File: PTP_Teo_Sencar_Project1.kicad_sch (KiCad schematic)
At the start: 0 parts

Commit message: Ispunjena sastavnica
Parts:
- added R1, R2: R_Small, symbol Device:R_Small
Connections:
- new net +3.3V: R2.1
- new net GND: R1.2
- new net U_izl: R1.1, R2.2
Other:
- company: (none) -> TVZ
- title: (none) -> BCD brojač

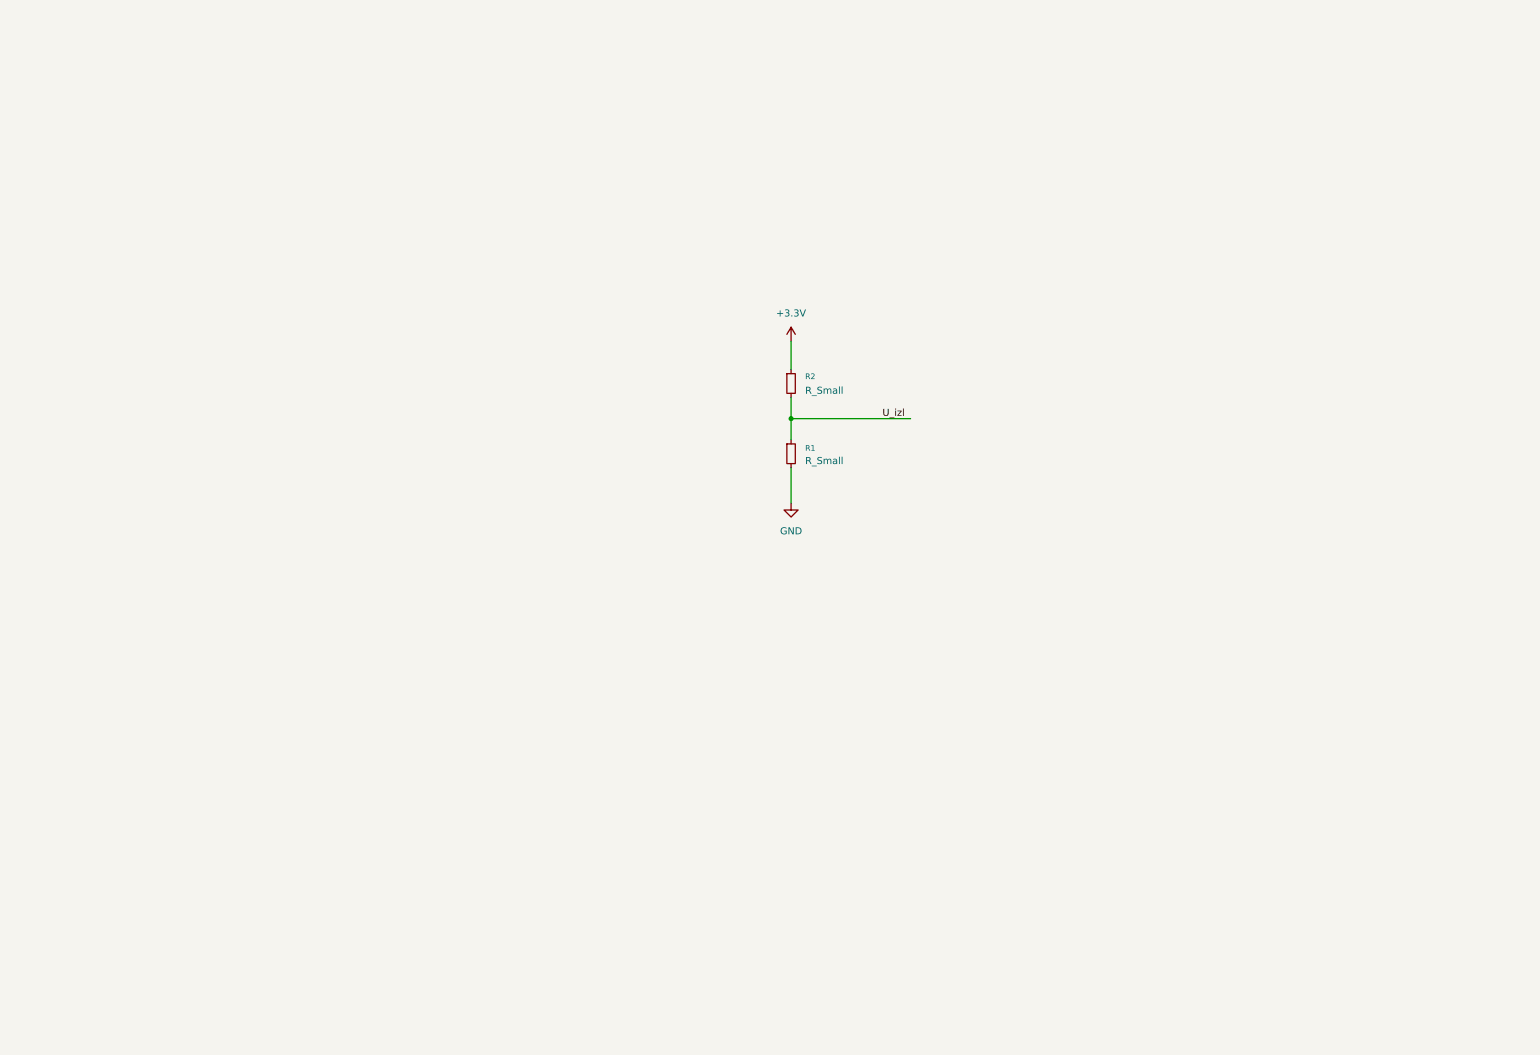
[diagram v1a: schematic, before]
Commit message: Dodan NE555
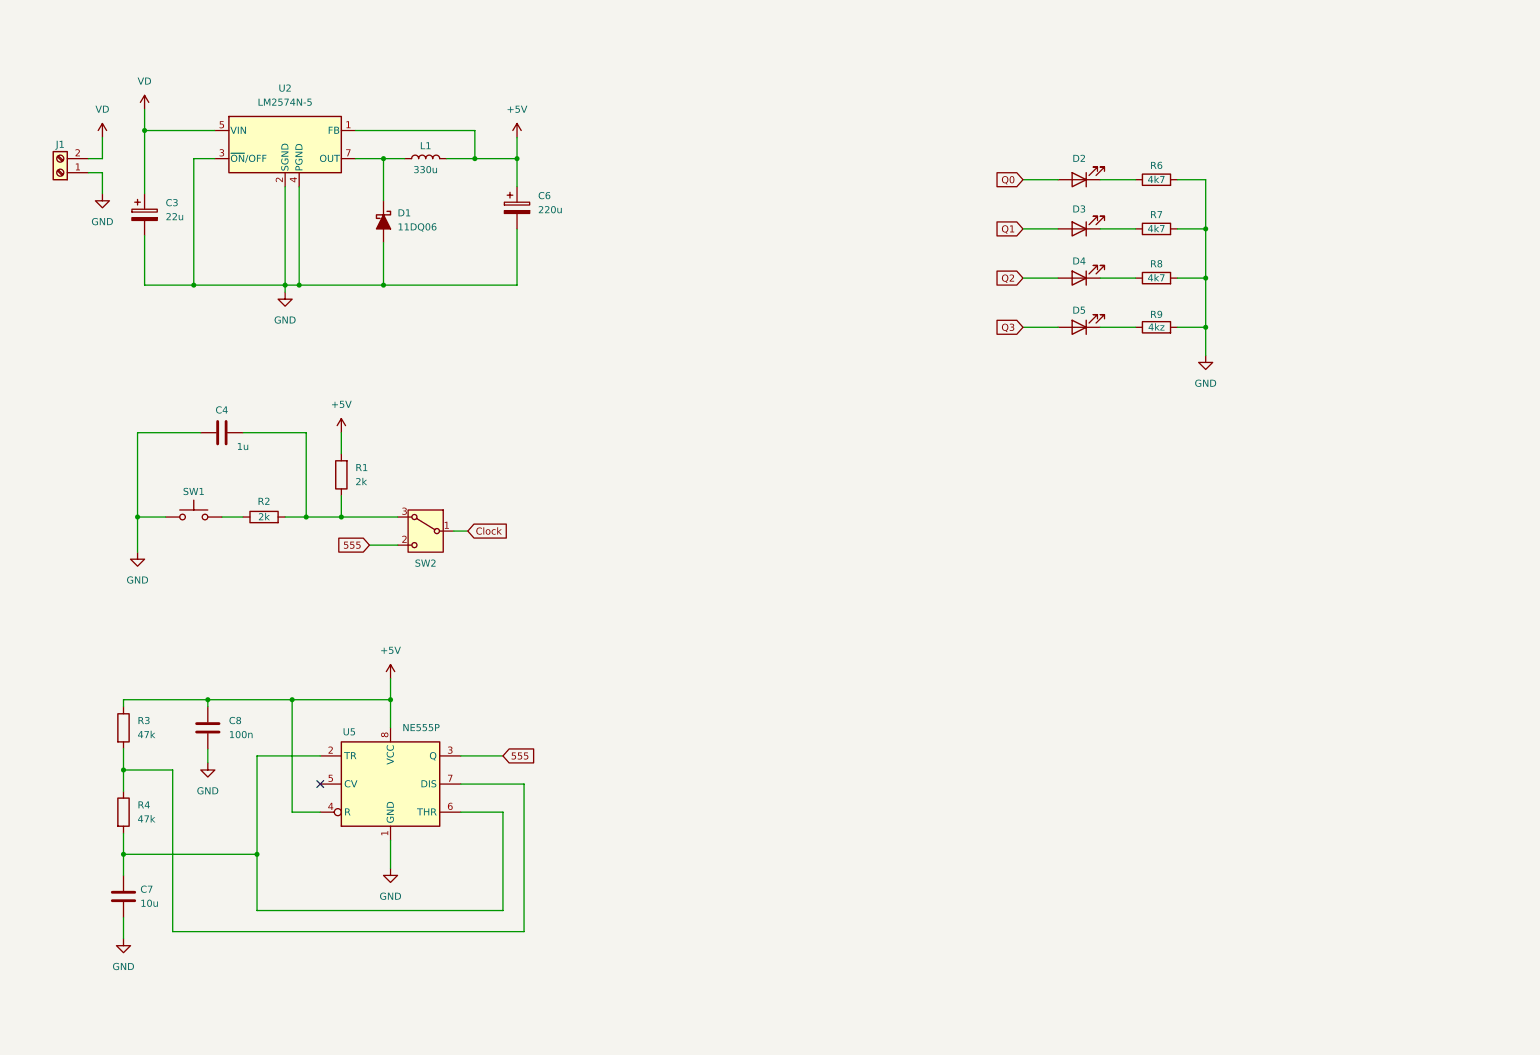
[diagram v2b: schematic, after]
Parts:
- removed R1, R2: R_Small, symbol Device:R_Small
- added C3: 22u, symbol Device:C_Polarized
- added C4: 1u, symbol Device:C
- added C6: 220u, symbol Device:C_Polarized
- added C7: 10u, symbol Device:C
- added C8: 100n, symbol Device:C
- added D1: 11DQ06, symbol Device:D_Schottky_Filled
- added D2, D3, D4, D5: LED, symbol Device:LED
- added J1: Screw_Terminal_01x02, symbol Connector:Screw_Terminal_01x02
- added L1: 330u, symbol Device:L
- added R1, R2: 2k, symbol Device:R
- added R3, R4: 47k, symbol Device:R
- added R6, R7, R8: 4k7, symbol Device:R
- added R9: 4kz, symbol Device:R
- added SW1: SW_Push, symbol Switch:SW_Push
- added SW2: SW_SPDT_312, symbol Switch:SW_SPDT_312
- added U2: LM2574N-5, Package_DIP:DIP-8_W7.62mm, symbol Regulator_Switching:LM2574N-5
- added U5: NE555P, Package_DIP:DIP-8_W7.62mm, symbol Timer:NE555P
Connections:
- net GND: now also C3.2, C4.1, C6.2, C7.2, C8.2, D1.2 (A), J1.1 (Pin_1), R6.2, R7.2, R8.2, R9.2, SW1.1, U2.2 (SGND), U2.3 (~{ON}/OFF), U2.4 (PGND), U5.1 (GND)
- new net: R2.1, SW1.2
- new net: R3.2, R4.1, U5.7 (DIS)
- new net: C7.1, R4.2, U5.2 (TR), U5.6 (THR)
- new net: C4.2, R1.1, R2.2, SW2.3 (A)
- new net: D1.1 (K), L1.1, U2.7 (OUT)
- new net: D4.1 (K), R8.1
- new net: D3.1 (K), R7.1
- new net: D2.1 (K), R6.1
- new net: D5.1 (K), R9.1
- new net +5V: C6.1, C8.1, L1.2, R1.2, R3.1, U2.1 (FB), U5.4 (R), U5.8 (VCC)
- new net 555: SW2.2 (C), U5.3 (Q)
- new net Clock: SW2.1 (B)
- new net Q0: D2.2 (A)
- new net Q1: D3.2 (A)
- new net Q2: D4.2 (A)
- new net Q3: D5.2 (A)
- new net VD: C3.1, J1.2 (Pin_2), U2.5 (VIN)
- no-connect marks 0 -> 1

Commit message: Footprint i simbol
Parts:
- removed C4: 1u, symbol Device:C
- removed R1, R2: 2k, symbol Device:R
- added C3: 1u, symbol Device:C
- added R13: 2k, symbol Device:R
- added R7: 10K, symbol Device:R
- added U6: 74LVC1G11, SOT-23-6:SOT-23-6, symbol SN74LVC1G11:SN74LVC1G11
- renumbered C3 to C1, C6 to C2, D2 to D1, D3 to D2, D4 to D3, D5 to D4, R6 to R1, R7 to R2, R8 to R3, R9 to R4, U2 to U1
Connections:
- net +5V: now also R7.2, U6.5 (VCC)
- net Clock: now also R7.1, U6.3 (B)
- net GND: now also C3.1, U6.2 (GND)
- net Q1: now also U6.6 (C)
- net Q3: now also U6.1 (A)
- net at SW1.2: now also R13.1
- net at SW2.3 (A): now also C3.2, R13.2
- new net Reset: U6.4 (Y)

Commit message: Popunjeni parametri komponenata
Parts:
- added H1, H2, H3, H4: MountingHole, symbol Mechanical:MountingHole
- added R10, R11, R12, R9: 10K, symbol Device:R
- added R14, R16, R17, R18, R5, R6, R8: 2k, symbol Device:R
- added R15: 10k, symbol Device:R
- added U2, U3: 4027, symbol 4xxx:4027
- added U4: 74LS47, symbol 74xx:74LS47
- added U5: FYS-3911BUHR-21, Display_7Segment:HDSP-7401, symbol Display_Character:HDSP-7401
- C1: footprint (none) -> Capacitor_THT:CP_Radial_D5.0mm_P2.00mm; Manufacturer (none) -> AISHI; Manufacturer Part Number (none) -> EWH1EM220D11OT
- C2: footprint (none) -> Capacitor_THT:CP_Radial_D5.0mm_P2.00mm; Manufacturer (none) -> SAMWHA; Manufacturer Part Number (none) -> RD1A227M05011BB
- C3: footprint (none) -> Capacitor_SMD:C_1206_3216Metric_Pad1.33x1.80mm_HandSolder; Manufacturer (none) -> SAMSUNG; Manufacturer Part Number (none) -> CL31B105KBHNNNE
- C4: renamed from C8; footprint (none) -> Capacitor_SMD:C_1206_3216Metric_Pad1.33x1.80mm_HandSolder; Manufacturer (none) -> SAMSUNG; Manufacturer Part Number (none) -> CL31B104KBCNNNC
- C5: renamed from C7; footprint (none) -> Capacitor_SMD:C_1206_3216Metric_Pad1.33x1.80mm_HandSolder; Manufacturer (none) -> SAMSUNG; Manufacturer Part Number (none) -> CL31A106KBHNNNE
- D1, D2, D3: footprint (none) -> LED_THT:LED_D5.0mm
- D4: renamed from D1; footprint (none) -> Diode_THT:D_DO-41_SOD81_P12.70mm_Horizontal; Manufacturer (none) -> SMC DIODE SOLUTIONS; Manufacturer Part Number (none) -> 11DQ06TA
- D5: renamed from D4; footprint (none) -> LED_THT:LED_D5.0mm
- renumbered R3 to R19, R4 to R20, U5 to U7
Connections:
- net +5V: now also R10.2, R11.2, R12.2, R15.1, R9.2, U2.16 (VDD), U3.16 (VDD), U4.16 (VCC), U5.1 (CA), U5.6 (CA)
- net Clock: now also U2.3 (C)
- net GND: now also U2.7 (S), U2.8 (VSS), U2.9 (S), U3.7 (S), U3.8 (VSS), U3.9 (S), U4.8 (GND)
- net Q0: now also U2.1 (Q), U2.13 (C), U4.7 (A)
- net Q1: now also U2.15 (Q), U3.3 (C), U4.1 (B)
- net Q2: now also U3.1 (Q), U3.13 (C), U4.2 (C)
- net Q3: now also U3.15 (Q), U4.6 (D)
- net Reset: now also U2.12 (R), U2.4 (R), U3.12 (R), U3.4 (R)
- new net: R6.1, U4.12 (b)
- new net: R6.2, U5.9 (B)
- new net: R5.2, U5.10 (A)
- new net: R17.2, U5.2 (F)
- new net: R18.2, U5.3 (G)
- new net: R16.2, U5.4 (E)
- new net: R14.2, U5.5 (D)
- new net: R8.2, U5.8 (C)
- new net: R15.2, U4.3 (LT), U4.4 (BI), U4.5 (RBI)
- new net: R12.1, U3.10 (J), U3.11 (K)
- new net: R5.1, U4.13 (a)
- new net: R16.1, U4.9 (e)
- new net: R10.1, U2.10 (J), U2.11 (K)
- new net: R18.1, U4.14 (g)
- new net: R14.1, U4.10 (d)
- new net: R17.1, U4.15 (f)
- new net: R11.1, U3.5 (K), U3.6 (J)
- new net: R9.1, U2.5 (K), U2.6 (J)
- new net: R8.1, U4.11 (c)
- no-connect marks 1 -> 6
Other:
- note added: "555 Timer"
- note added: "JK bistabil"
- note added: "LED diode"
- note added: "Montažne rupe"
- note added: "Napajanje"
- note added: "Napajanje bistabila"
- note added: "Reset brojača"
- note added: "Tipkalo i ulaz radnog takta"
- moved on the sheet: C1, C2, C3, C4, C5, D1, D2, D3, D4, D5, J1, L1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

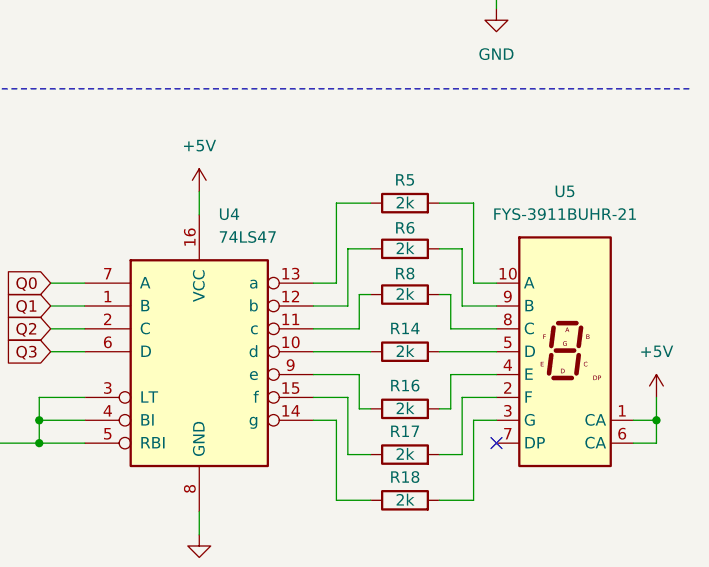
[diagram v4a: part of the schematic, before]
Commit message: Dovršeni footprinti
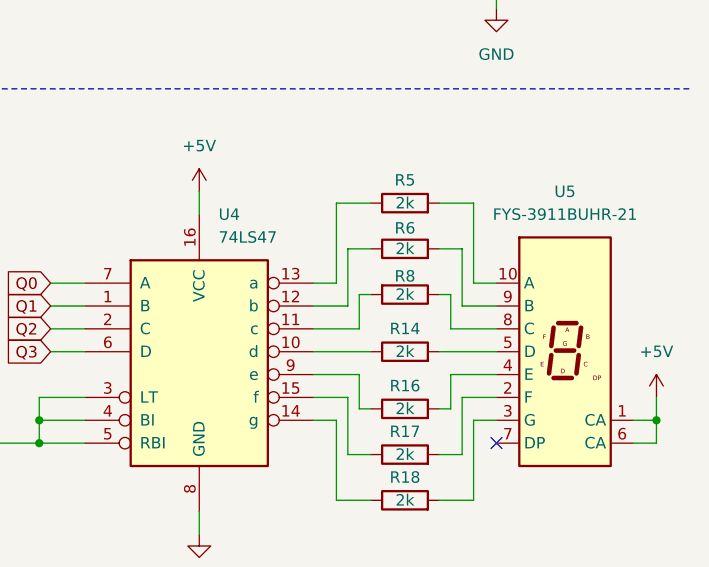
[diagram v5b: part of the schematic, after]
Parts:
- H1, H2, H3, H4: footprint (none) -> MountingHole:MountingHole_5.5mm
- J1: footprint (none) -> TerminalBlock_MetzConnect:TerminalBlock_MetzConnect_Type011_RT05502HBLC_1x02_P5.00mm_Horizontal; Manufacturer (none) -> DEGSON ELECTRONICS; Manufacturer Part Number (none) -> DG301-5.0-02P-12-00A(H)
- L1: footprint (none) -> Inductor_THT:L_Radial_D7.2mm_P3.00mm_Murata_1700; Manufacturer (none) -> FERROCORE; Manufacturer Part Number (none) -> COIL0608-0.33
- R1, R2, R3, R4: footprint (none) -> Resistor_THT:R_Axial_DIN0207_L6.3mm_D2.5mm_P10.16mm_Horizontal
- R10, R11, R12, R15, R7, R9: footprint (none) -> Resistor_SMD:R_1206_3216Metric_Pad1.30x1.75mm_HandSolder
- R13, R14, R16, R17, R5, R6, R8: footprint (none) -> Resistor_SMD:R_1206_3216Metric_Pad1.30x1.75mm_HandSolder; Manufacturer (none) -> ROYALOHM; Manufacturer Part Number (none) -> 1206S4F2001T5E
- R18: footprint (none) -> Resistor_SMD:R_1206_3216Metric_Pad1.30x1.75mm_HandSolder; Manufacturer (none) -> ROYALOHM; Manufacturer Part Number (none) -> Resistor_SMD:R_1206_3216Metric_Pad1.30x1.75mm_HandSolder
- R19, R20: footprint (none) -> Resistor_SMD:R_1206_3216Metric_Pad1.30x1.75mm_HandSolder; Manufacturer (none) -> ROYALOHM; Manufacturer Part Number (none) -> 1206S4J0473T5E
- SW1: footprint (none) -> Button_Switch_THT:SW_PUSH_6mm_H4.3mm; Manufacturer (none) -> microswitch TACT; Manufacturer Part Number (none) -> TACT-64N-F
- SW2: footprint (none) -> Button_Switch_THT:SW_Slide_SPDT_Straight_CK_OS102011MS2Q; Manufacturer (none) -> C&K; Manufacturer Part Number (none) -> OS102011MS2QN1C
- U1: footprint Package_DIP:DIP-8_W7.62mm -> Package_DIP:DIP-8_W7.62mm_Socket_LongPads; Manufacturer (none) -> ONSEMI; Manufacturer Part Number (none) -> LM2574N-5G
- U2, U3: footprint (none) -> Package_DIP:DIP-16_W7.62mm_Socket_LongPads; Manufacturer (none) -> RENESAS; Manufacturer Part Number (none) -> CD4027BMS
- U4: footprint (none) -> Package_DIP:DIP-16_W7.62mm_Socket_LongPads; Manufacturer (none) -> TEXAS INSTRUMENTS; Manufacturer Part Number (none) -> SN74LS47N
- U5: Manufacturer (none) -> FORYARD; Manufacturer Part Number (none) -> FYS-3911BUHR-21
- U6: footprint SOT-23-6:SOT-23-6 -> Package_TO_SOT_SMD:SOT-23-6; Manufacturer (none) -> TEXAS INSTRUMENTS; Manufacturer Part Number (none) -> SN74LVC1G11DBVR
- U7: Manufacturer (none) -> TEXAS INSTRUMENTS; Manufacturer Part Number (none) -> NE555P
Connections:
- net at U5.8 (C): now also R8.1; no longer R8.2
- net at U4.11 (c): now also R8.2; no longer R8.1
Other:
- moved on the sheet: R8

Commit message: Gerber fileovi, BOM
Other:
- moved on the sheet: C3, R13, R7, SW1, SW2
